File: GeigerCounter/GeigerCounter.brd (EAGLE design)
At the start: 100 x 80 mm, 45 parts, among them IC1 OPAMP-DUALU, IC2 OPAMP-DUALU

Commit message: Revised schematic based on working breadboard. Changed footprints to SMD pads.
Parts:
- removed C10, C11, C8: 0.1uF, SparkFun-Passives:CAP-PTH-SMALL2
- removed C9: 2.2uF, SparkFun-Passives:CAP-PTH-SMALL2
- removed IC2: OPAMP-DUALU, SparkFun-AnalogIC:SO08
- removed R16: 10k, SparkFun-Passives:AXIAL-0.3
- removed R18: DNP, SparkFun-Passives:AXIAL-0.3
- removed R19: 100k, SparkFun-Passives:AXIAL-0.3
- removed R25: 0, SparkFun-Passives:AXIAL-0.3
- removed TP_INV1, TP_INV2, TP_POS1, TP_POS2: PTR1PAD1-20, testpad:P1-20
- removed U$2, U$3: M04X2, SparkFun-Connectors:2X4
- added D2: DNP, SparkFun-DiscreteSemi:SOT23-3
- added R9: 0, SparkFun-Passives:0603-RES
- added TP_AMP, TP_ENV, TP_GND1, TP_GND2, TP_PRE_AMP, TP_RC, TP_VBIAS, TP_VCC1: PTR1PAD1-20, testpad:P1-20
- C1: value DNP -> 15pF; device SparkFun-Passives:CAP-PTH-SMALL2 -> SparkFun-Passives:0603-CAP
- C2: value 2pF -> 100p; device SparkFun-Passives:CAP-PTH-SMALL2 -> SparkFun-Passives:0603-CAP
- C3: value 100pF -> 0.1u; device SparkFun-Passives:CAP-PTH-SMALL2 -> SparkFun-Passives:0603-CAP
- C4: value 2pF -> DNP; device SparkFun-Passives:CAP-PTH-SMALL2 -> SparkFun-Passives:0603-CAP
- C5: value 100pF -> DNP; device SparkFun-Passives:CAP-PTH-SMALL2 -> SparkFun-Passives:0603-CAP
- C6: value DNP -> 2.2uF; device SparkFun-Passives:CAP-PTH-SMALL2 -> SparkFun-Passives:0603-CAP
- C7: value 2.2uF -> 0.1uF; device SparkFun-Passives:CAP-PTH-SMALL2 -> SparkFun-Passives:0603-CAP
- R1: value 1k -> 10M; device SparkFun-Passives:AXIAL-0.3 -> SparkFun-Passives:0603-RES
- R10, R14: value 10 MEGA -> 0; device SparkFun-Passives:AXIAL-0.3 -> SparkFun-Passives:0603-RES
- R11, R13, R15, R2, R6, R8: device SparkFun-Passives:AXIAL-0.3 -> SparkFun-Passives:0603-RES
- R12: value DNP -> 0; device SparkFun-Passives:AXIAL-0.3 -> SparkFun-Passives:0603-RES
- R3: value 10k -> 0; device SparkFun-Passives:AXIAL-0.3 -> SparkFun-Passives:0603-RES
- R4: value 1k -> 100; device SparkFun-Passives:AXIAL-0.3 -> SparkFun-Passives:0603-RES
- R5: value DNP -> 100; device SparkFun-Passives:AXIAL-0.3 -> SparkFun-Passives:0603-RES
- R7: value 0 -> DNP; device SparkFun-Passives:AXIAL-0.3 -> SparkFun-Passives:0603-RES
- moved TP_GND 230.2 mm to (10.6, 61.4)
- moved TP_VCC 230.2 mm to (10.6, 66.5)
- moved C1 150.8 mm to (1.40, -1.32)
- moved H1 127.7 mm to (93.1, 19.6)
- moved H2 127.7 mm to (85.0, 19.6)
- moved H3 127.7 mm to (76.8, 19.6)
- moved H4 127.7 mm to (68.7, 19.6)
- moved C6 125.9 mm to (1.40, -36.4)
- moved C7 92.0 mm to (1.40, -38.7)
- moved R8 91.1 mm to (1.40, -29.4)
- moved D1 89.2 mm to (72.2, 47.7)
- moved U$1 89.2 mm to (69.9, 42.4)
- moved R13 71.9 mm to (1.37, -57.3)
- moved C4 70.8 mm to (1.40, -8.33)
- moved C5 65.1 mm to (1.40, -10.7)
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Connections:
- removed net N$1: C3.2, R3.P$1
- removed net N$10: C4.2, IC2.1, R12.P$2, R14.P$2, R15.P$1
- removed net N$11: C4.1, IC2.2, R12.P$1, R14.P$1, U$2.8
- removed net N$12: C5.1, R15.P$2, TP_POS1.TP
- removed net N$13: C5.2, R13.P$1
- removed net N$14: IC2.6, R18.P$1, R19.P$1, R8.P$2
- removed net N$15: IC2.7, R18.P$2, R19.P$2, R25.P$1, TP_POS2.TP
- removed net N$16: C6.1, R7.P$2, U$3.1, U$3.3
- removed net N$17: C1.1, R25.P$2, U$3.5, U$3.7
- removed net N$2: D1.C, U$2.5, U$2.7
- removed net N$3: C2.2, IC1.1, R10.P$2, R11.P$1, R2.P$2
- removed net N$4: IC2.5, R13.P$2, R16.P$2
- removed net N$5: D1.A, U$2.1, U$2.3
- removed net N$6: C2.1, IC1.2, R10.P$1, R2.P$1, U$2.2
- removed net N$7: C3.1, R11.P$2, TP_INV1.TP
- removed net N$8: IC1.6, R3.P$2, R5.P$1, R6.P$1
- removed net N$9: IC1.7, R5.P$2, R6.P$2, R7.P$1, TP_INV2.TP
- new net ENV_DETEC_OUT: C4.1, D2.3, R11.2, R9.1, TP_ENV.TP
- new net IC1A_N: C1.1, D1.A, IC1.2, R1.2, R2.2
- new net IC1A_OUT: C1.2, IC1.1, R1.1, R2.1, R3.2
- new net IC1B_N: IC1.6, R6.1, R7.1, R8.2
- new net IC1B_OUT: D2.1, IC1.7, R11.1, R6.2, R7.2, TP_AMP.TP
- new net INV_AMP_INPUT: C2.2, R8.1
- new net OUTPUT: R10.2, R12.1, R13.1, R14.1, R15.1
- new net PRE_AMP: C2.1, R3.1, TP_PRE_AMP.TP
- new net RC_OUT: C5.1, R10.1, R9.2, TP_RC.TP
- net GND: now also C3.1, C4.2, C5.2, C7.2, R4.2, TP_GND1.TP, TP_GND2.TP; no longer C1.2, C10.1, C11.1, C7.1, C8.1, C9.1, IC2.3, IC2.4, R1.P$1, R16.P$1, R8.P$1, U$2.4
- net NC1: now also R13.2; no longer U$3.2
- net NC2: now also R14.2; no longer U$3.6
- net P3.4: now also R15.2; no longer U$3.8
- net P3.5: now also R12.2; no longer U$3.4
- net VCC: now also C6.1, C7.1, R5.1, TP_VCC1.TP; no longer C10.2, C7.2, C8.2, C9.2, IC2.8, R4.P$2
- net VCC_1.25: now also C3.2, D1.C, R4.1, R5.2, TP_VBIAS.TP; no longer C11.2, R1.P$2, R4.P$1, U$2.6

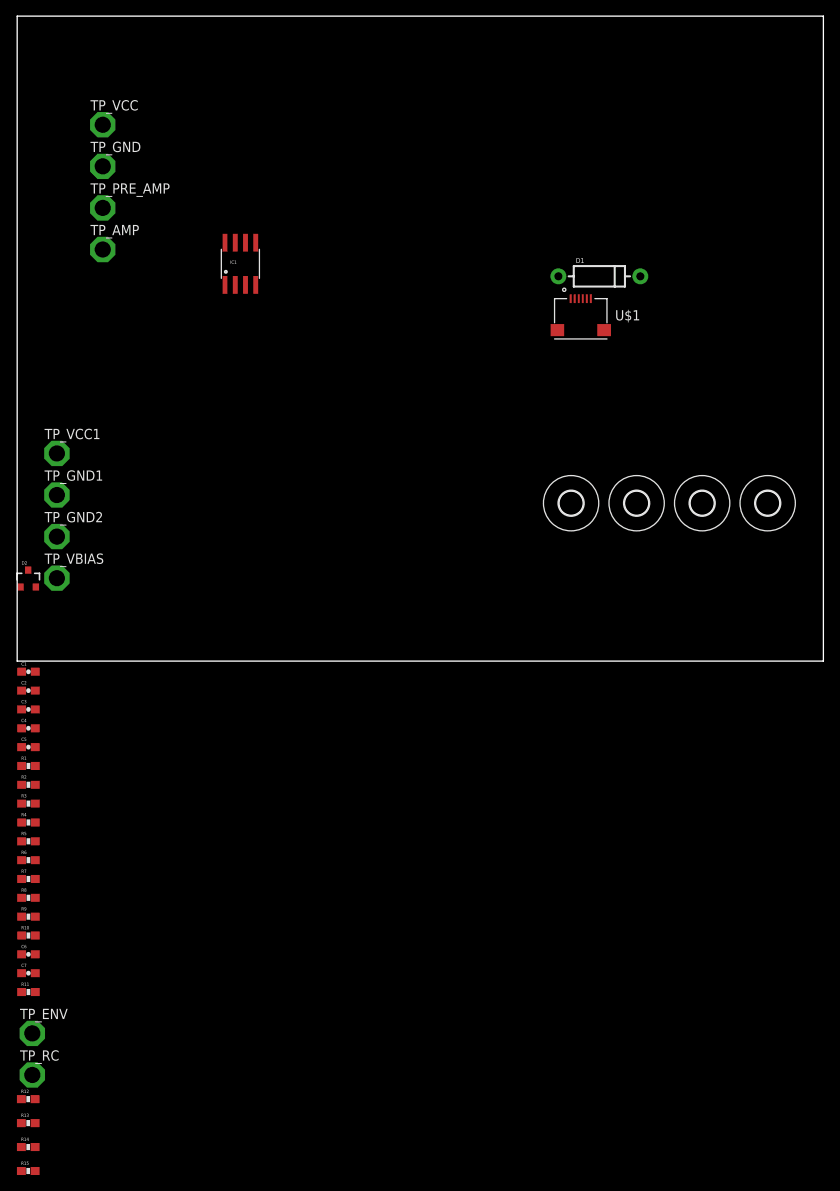
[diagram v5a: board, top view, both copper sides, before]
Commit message: Layout completed. Routed not yet started.
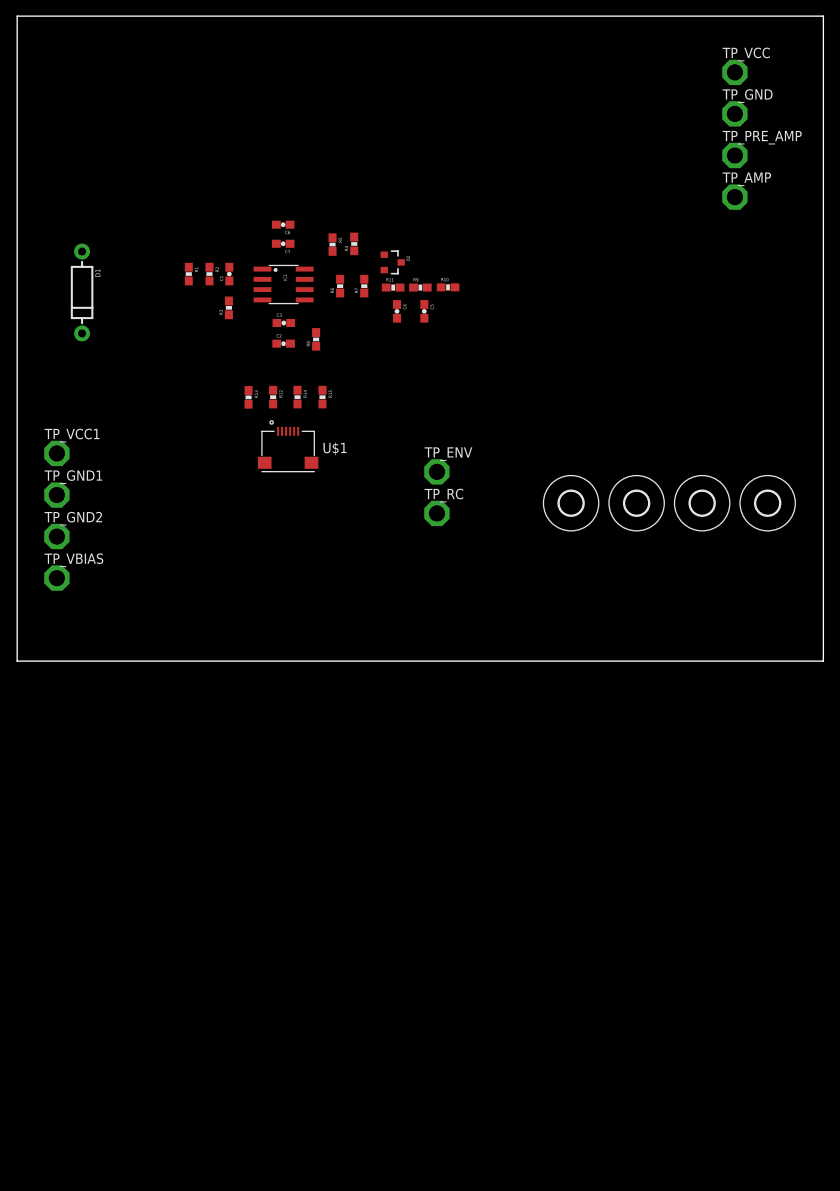
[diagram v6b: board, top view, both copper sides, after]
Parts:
- moved R15 102.7 mm to (37.9, 32.7), turned to 270 degrees
- moved R14 98.8 mm to (34.8, 32.7), turned to 270 degrees
- moved R11 98.4 mm to (46.6, 46.3)
- moved C6 95.9 mm to (33.0, 54.1), turned to 180 degrees
- moved C7 95.8 mm to (33.0, 51.8), turned to 180 degrees
- moved R10 95.8 mm to (53.4, 46.4)
- moved R13 94.1 mm to (28.7, 32.7), turned to 270 degrees
- moved R12 92.2 mm to (31.8, 32.7), turned to 270 degrees
- moved R9 91.9 mm to (50.0, 46.3)
- moved TP_ENV 85.8 mm to (52.1, 23.5)
- moved TP_RC 85.8 mm to (52.1, 18.3)
- moved R7 84.5 mm to (43.1, 46.5), turned to 90 degrees
- moved R5 83.1 mm to (39.1, 51.7), turned to 270 degrees
- moved R4 82.4 mm to (41.8, 51.7), turned to 90 degrees
- moved R6 81.0 mm to (40.1, 46.5), turned to 90 degrees
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
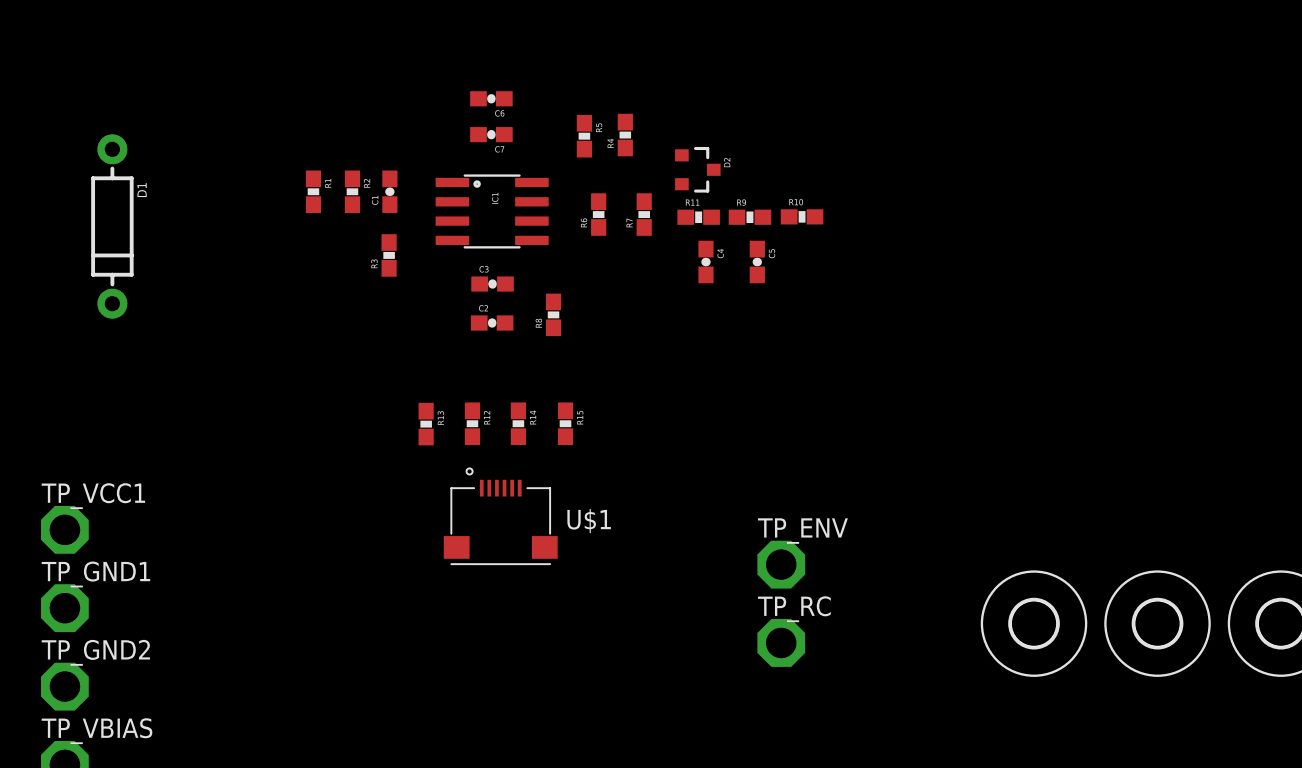
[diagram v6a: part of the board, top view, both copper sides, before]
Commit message: Basic routing completed. No pours yet.
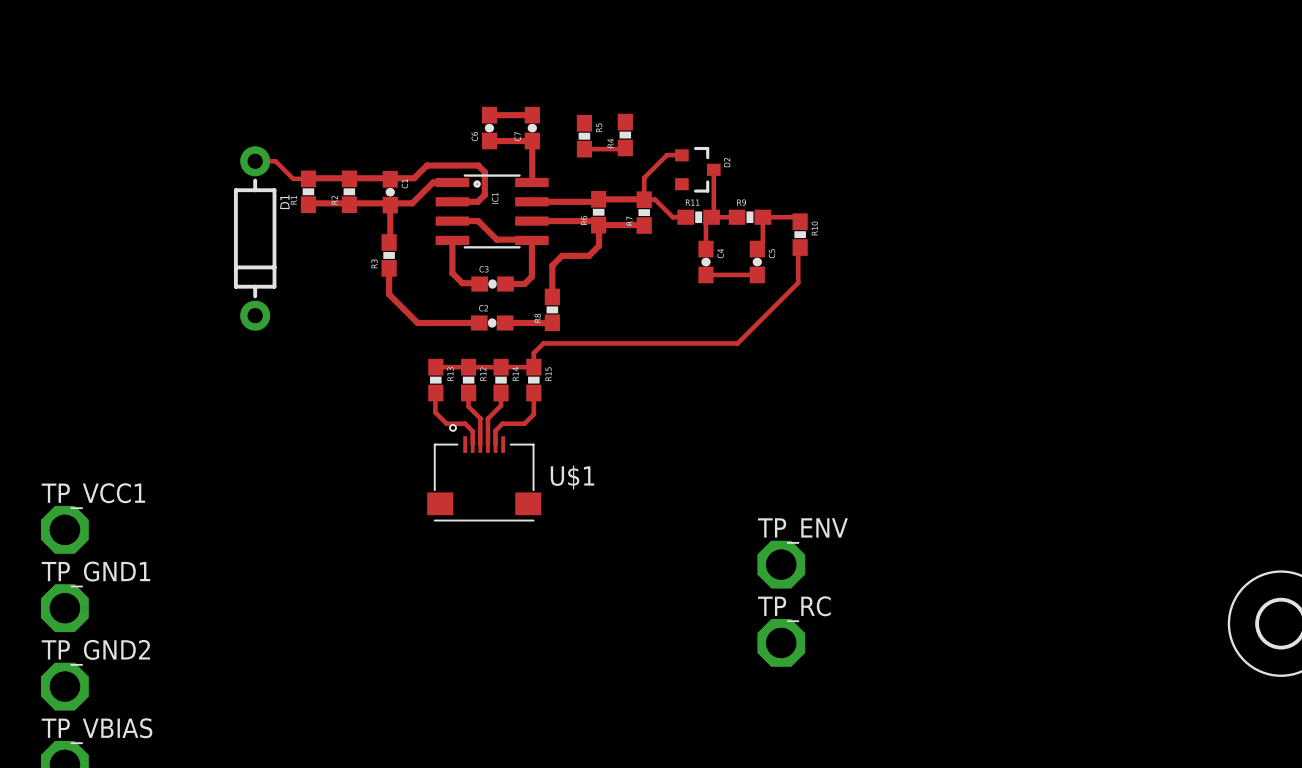
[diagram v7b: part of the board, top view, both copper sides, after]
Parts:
- removed H3, H4: MOUNT-HOLE3.0, holes:3,0
- moved D1 9.43 mm to (17.4, 44.9)
- moved R15 3.55 mm to (35.8, 35.6)
- moved R14 3.09 mm to (33.6, 35.6)
- moved U$1 3.07 mm to (32.5, 28.8)
- moved R13 2.96 mm to (29.3, 35.6)
- moved R12 2.88 mm to (31.5, 35.6)
- moved C7 2.73 mm to (35.7, 52.2), turned to 90 degrees
- moved C6 1.93 mm to (32.9, 52.2), turned to 90 degrees
- moved R10 1.18 mm to (53.3, 45.2), turned to 270 degrees
- moved R8 0.34 mm to (37.0, 40.2)
- moved R1 0.33 mm to (21.0, 48.0), turned to 90 degrees
- moved R2 0.20 mm to (23.6, 48.0), turned to 90 degrees
- moved R6 0.15 mm to (40.1, 46.7)
- moved R7 0.13 mm to (43.1, 46.6)
- turned C1 to 270 degrees
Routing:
- net OUTPUT: track 0.00 -> 29.1 mm
- net IC1A_N: track 0.00 -> 20.0 mm
- net IC1B_OUT: track 0.00 -> 15.2 mm
- net IC1B_N: track 0.00 -> 14.6 mm
- net VCC_1.25: track 0.00 -> 12.8 mm
- net IC1A_OUT: track 0.00 -> 12.6 mm
- net GND: track 0.00 -> 10.4 mm
- net PRE_AMP: track 0.00 -> 8.43 mm
- net ENV_DETEC_OUT: track 0.00 -> 7.11 mm
- net VCC: track 0.00 -> 5.56 mm
- net P3.4: track 0.00 -> 5.28 mm
- net NC1: track 0.00 -> 5.13 mm
- net RC_OUT: track 0.00 -> 4.82 mm
- net NC2: track 0.00 -> 3.75 mm
- net P3.5: track 0.00 -> 3.71 mm
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
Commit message: More routing
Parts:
- removed TP_GND2: PTR1PAD1-20, testpad:P1-20
- moved H1 81.2 mm to (20.7, 56.4)
- moved TP_GND 74.9 mm to (20.2, 38.4)
- moved TP_PRE_AMP 65.9 mm to (27.8, 38.4)
- moved TP_VCC 54.5 mm to (46.8, 38.5)
- moved H2 52.1 mm to (48.1, 56.4)
- moved TP_VCC1 40.2 mm to (43.0, 38.5)
- moved TP_AMP 39.2 mm to (50.6, 49.8)
- moved TP_VBIAS 36.8 mm to (22.1, 42.8)
- moved TP_GND1 26.1 mm to (24.0, 38.4)
- moved TP_ENV 21.4 mm to (41.8, 42.2)
- moved TP_RC 20.1 mm to (50.6, 38.4)
- moved R10 3.73 mm to (50.5, 42.7)
- moved C5 2.67 mm to (47.9, 42.7)
- moved R12 1.86 mm to (33.3, 35.3)
- moved U$1 1.86 mm to (34.4, 28.5)
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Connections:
- net GND: no longer TP_GND2.TP
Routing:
- net OUTPUT: track 29.1 -> 6.45 mm
- net ENV_DETEC_OUT: track 7.11 -> 9.15 mm
- net PRE_AMP: track 8.43 -> 7.42 mm
- net GND: track 10.4 -> 9.58 mm
- net RC_OUT: track 4.82 -> 5.48 mm
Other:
- board size 100 x 80 mm -> 38.1 x 35.6 mm
